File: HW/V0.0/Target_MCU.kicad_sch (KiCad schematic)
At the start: 18 parts, among them SW1 SW-2P, U3 PIC16F877A-I/PT

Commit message: PIC16-DevKit-SCH-877 schematic update 4
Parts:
- added MD1: ARDUINO-UNO-R3, symbol SAMPI:ARDUINO-UNO-R3
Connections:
- net GND: now also MD1.29 (GND), MD1.6 (GND), MD1.7 (GND)
- new net +3.3V: MD1.4 (+3V3)
- new net +5V: MD1.5 (+5V)
- new net VDC: MD1.8 (VIN)

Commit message: PIC16-DevKit-SCH-877 schematic update 5
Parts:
- removed C18: 100nF, symbol Triet_KiCAD_Sym:CAP_CER
- removed R25: 330R, symbol Triet_KiCAD_Sym:RES
- removed Y2: ~, symbol Triet_KiCAD_Sym:Crystal-3P
- added J3: EXP PORT, SAMPI:HDM1x10x2.54_TH_RA, symbol SAMPI:SIL10
- added R11, R12, R14, R15, R16, R19, R20: 330R, SAMPI:RES0603, symbol Triet_KiCAD_Sym:RES
- added U10: 20MHz, SAMPI:CDFN3225-4LD-PL-1, symbol SAMPI:XTAL-4P
- C15: renamed from C16; footprint (none) -> SAMPI:CAP0603
- C16: renamed from C15; footprint (none) -> SAMPI:CAP0603
- C17: footprint (none) -> SAMPI:CAP0603
- C18: renamed from C8; footprint (none) -> SAMPI:CAP0603
- C19: renamed from C9; footprint (none) -> SAMPI:CAP0603
- C20: renamed from C10; footprint (none) -> SAMPI:CAP0603
- C21: renamed from C11; footprint (none) -> SAMPI:CAP0603
- D5: renamed from D4; value PWR -> ULED; footprint (none) -> SAMPI:LED0603
- MD1: footprint (none) -> SAMPI:ARDUINO-UNO-R3
- R13: value 1k -> 330R; footprint (none) -> SAMPI:RES0603
- R17: value 10k -> 330R; footprint (none) -> SAMPI:RES0603
- R18: renamed from R16; value 10k -> 10K; footprint (none) -> SAMPI:RES0603
- R21: renamed from R34; value 4.7k -> 5.1K, 1%; footprint (none) -> SAMPI:RES0603
- R22: renamed from R35; value 4.7k -> 5.1K, 1%; footprint (none) -> SAMPI:RES0603
- SW1: value SW-2P -> UBT; MPN SW603625R2 -> (none)
- U4: renamed from U3; value PIC16F877A-I/PT -> PIC16F877A; footprint (none) -> SAMPI:TQFP44-10x10-P0.8; MFT (none) -> Microchip; MNP (none) -> PIC16F877A-I/PT
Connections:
- net AN4/SCL is gone; now on net GND: U4.6 (VSS)
- net AN5/SDA is gone; now on net +VDDTG: U4.7 (VDD)
- net GPIO2 is gone; now on net INT1: U4.9 (RB1)
- net GPIO3 is gone; now on net INT0: U4.8 (INT/RB0)
- net GPIO5 is gone; now on net SCL: U4.37 (SCK/SCL/RC3)
- net MOSI is gone; now on net AN4: U4.24 (~{SS}/C2OUT/AN4/RA5)
- net RESET is gone; now on net INT2: U4.10 (RB2)
- net RTC_CLKO is gone; now on net SCLK: U4.15 (RB5)
- net RTC_EVI is gone; now on net AN1: U4.20 (AN1/RA1)
- net TG_RXD is gone; now on net ~{UBT}: U4.26 (RE1/~{WR}/AN6)
- net TG_TXD is gone; now on net AN5: U4.25 (RE0/~{RD}/AN5)
- net UART_SEL is gone; now on net AN0: U4.19 (AN0/RA0)
- net ~{FLASH_CS} is gone; now on net AN3: U4.22 (VREF+/AN3/RA3)
- net ~{FLASH_WP} is gone; now on net AN2: U4.21 (CVREF/VREF-/AN2/RA2)
- net ~{RTC_INT} is gone; now on net PWM2: U4.35 (T1OSI/CCP2/RC1)
- net ~{TEMP_OS} is gone; now on net +VDDTG: U4.28 (VDD)
- net ~{TG_PGM}/~{SRAM_CS_3V3} is gone; now on net PWM1: U4.36 (CCP1/RC2)
- net +VDDTG: now also MD1.2 (IOREF), MD1.30 (AREF), J3.2; no longer R17.1, U4.11 (VDD), U4.32 (VDD)
- net AN0: now also MD1.9 (AN0); no longer U4.2 (AN0/RA0)
- net AN1: now also MD1.10 (AN1); no longer U4.3 (AN1/RA1)
- net AN2: now also MD1.11 (AN2); no longer U4.4 (CVref/Vref-/AN2/RA2)
- net AN3: now also MD1.12 (AN3); no longer U4.5 (Vref+/AN3/RA3)
- net GND: now also D5.K, U4.29 (VSS), J3.1, U10.2 (GND1), U10.4 (X2); no longer U4.12 (VSS), U4.31 (VSS)
- net INT0: now also MD1.21 (D6); no longer U4.34 (RB1)
- net INT1: now also MD1.22 (D7); no longer U4.33 (INT/RB0)
- net SCL: now also MD1.32 (D15/SCL); no longer U4.18 (SCK/SCL/RC3)
- net SCLK: now also MD1.28 (D13/SCLK); no longer U4.39 (PGC/RB6)
- net SDA: now also MD1.31 (D14/SDA), U4.42 (SDI/SDA/RC4); no longer U4.23 (SDI/SDA/RC4)
- net ~{CS}: now also MD1.25 (D10/~{SS}), U4.11 (PGM/RB3); no longer U4.27 (RD4/PSP4)
- net AN4: now reaches MD1.13 (AN4/SDA)
- net AN5: now reaches MD1.14 (AN5/SCL)
- net RXD: now reaches MD1.15 (D0/RXD)
- net RXD: now also U4.1 (DT/RX/RC7)
- net TXD: now reaches MD1.16 (D1/TXD)
- net TXD: now also U4.44 (CK/TX/RC6)
- net T0CKI: now reaches MD1.17 (D2)
- net T0CKI: now also U4.23 (C1OUT/T0CKI/RA4)
- net T1CKI: now reaches MD1.18 (D3)
- net T1CKI: now also U4.32 (T1OSO/T1CKI/RC0)
- net ULED: now reaches MD1.19 (D4)
- net ULED: now also U4.27 (RE2/~{CS}/AN7), R19.1
- net INT2: now reaches MD1.20 (D5)
- net PWM1: now reaches MD1.23 (D8)
- net PWM2: now reaches MD1.24 (D9)
- net SDO: now reaches MD1.26 (D11/MOSI)
- net SDO: now also U4.43 (SDO/RC5)
- net SDI: now reaches MD1.27 (D12/MISO)
- net SDI: now also U4.14 (RB4)
- net ~{MCLR}: now reaches MD1.3 (RESET)
- net ~{MCLR}: now also U4.18 (~{MCLR}/VPP)
- net at C15.2: now also U4.30 (OSC1/CLKI), U10.3 (GND2); no longer U4.13 (OSC1/CLKI)
- net ~{UBT}: now reaches C17.2, R18.2, SW1.B
- net ~{UBT}: no longer R13.2
- net at R17.2: now also J3.9; no longer U4.1 (~{MCLR}/Vpp)
- net at C16.2: now also U4.31 (OSC2/CLKO), U10.1 (X1); no longer U4.14 (OSC2/CLKO)
- net GPIO0 renamed PGC
- net GPIO1 renamed PGD
- net GPIO4 renamed RD0
- net RD0: now also R11.1
- net MISO renamed RD2
- net RD2: now also R13.1
- removed net USER_LED: D5.1 (A), U4.29 (RD6/PSP6)
- removed net ~{USER_BT}: R13.1, U4.30 (RD7/PSP7)
- new net: J3.10, R20.2
- new net: J3.3, R11.2
- new net: J3.4, R12.2
- new net: J3.5, R13.2
- new net: J3.6, R14.2
- new net: J3.7, R15.2
- new net: J3.8, R16.2
- new net: D5.A, R19.2
- new net RD1: R12.1, U4.39 (RD1/PSP1)
- new net RD3: R14.1, U4.41 (RD3/PSP3)
- new net RD4: R15.1, U4.2 (RD4/PSP4)
- new net RD5: R16.1, U4.3 (RD5/PSP5)
- new net RD6: R17.1, U4.4 (RD6/PSP6)
- new net RD7: R20.1, U4.5 (RD7/PSP7)
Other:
- moved on the sheet: C15, C16, C17, D5, R18, SW1

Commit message: PIC16-DevKit-SCH-877 schematic update 6
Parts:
- removed SW1: UBT, Triet_KiCAD_Fprint:SW_2P_3.5x6, symbol Triet_KiCAD_Sym:Switch_2P
- added BT2: UBT, Liem:SW6x6-G, symbol SAMPI:BT2
- C15, C16: MFT (none) -> Walsin; MNP (none) -> 0603N220J500CT
- C17, C18, C20: MFT (none) -> Samsung; MNP (none) -> CL10B104KB8NNNC
- C19, C21: MFT (none) -> Samsung; MNP (none) -> CL10A106MQ8NNNC
- D5: MFT (none) -> Harvatek; MNP (none) -> B1911NG--20D000214U1930
- J3: footprint SAMPI:HDM1x10x2.54_TH_RA -> SAMPI:HDM1x10x2.54_TH; MFT (none) -> Adam Tech; MNP (none) -> RS1-10-G
- MD1: MFT (none) -> JLCPCB; MNP (none) -> PCB.SAMM-877A
- R11, R12, R13, R14, R15, R16, R17, R19, R20: MFT (none) -> Yageo; MNP (none) -> RC0603JR-07330RL
- R18: MFT (none) -> Yageo; MNP (none) -> RC0603JR-0710KL
- R21, R22: MFT (none) -> Yageo; MNP (none) -> RC0603FR-075K1L
- U10: MFT (none) -> Diodes; MNP (none) -> FL2000038
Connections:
- net GND: now also BT2.3, BT2.4
- net ~{UBT}: now also BT2.1, BT2.2
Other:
- moved on the sheet: C17, R18

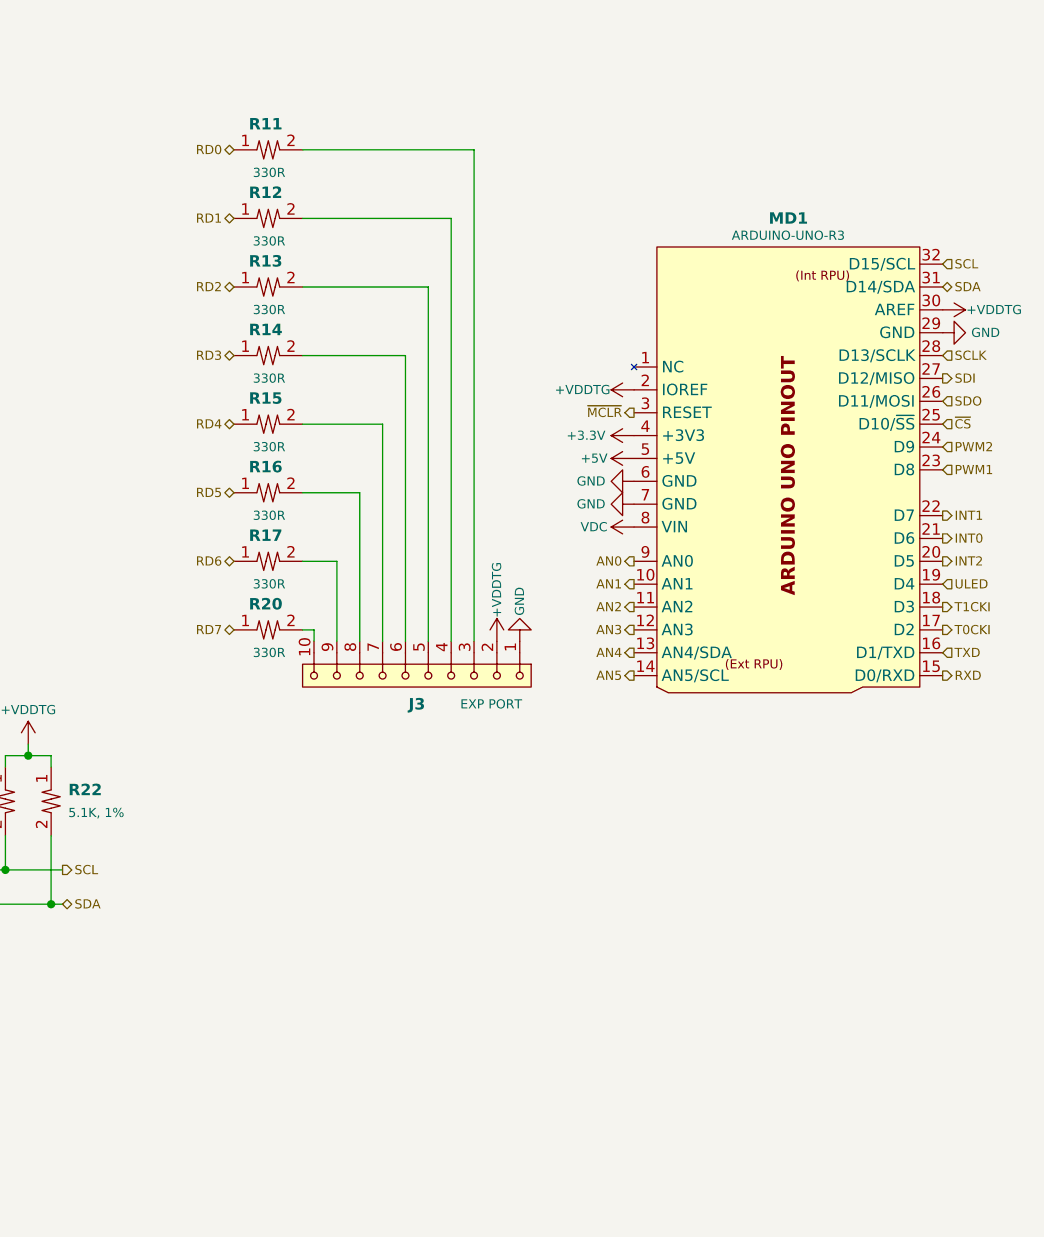
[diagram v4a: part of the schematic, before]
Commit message: PIC16-DevKit-SCH-877 schematic update 7
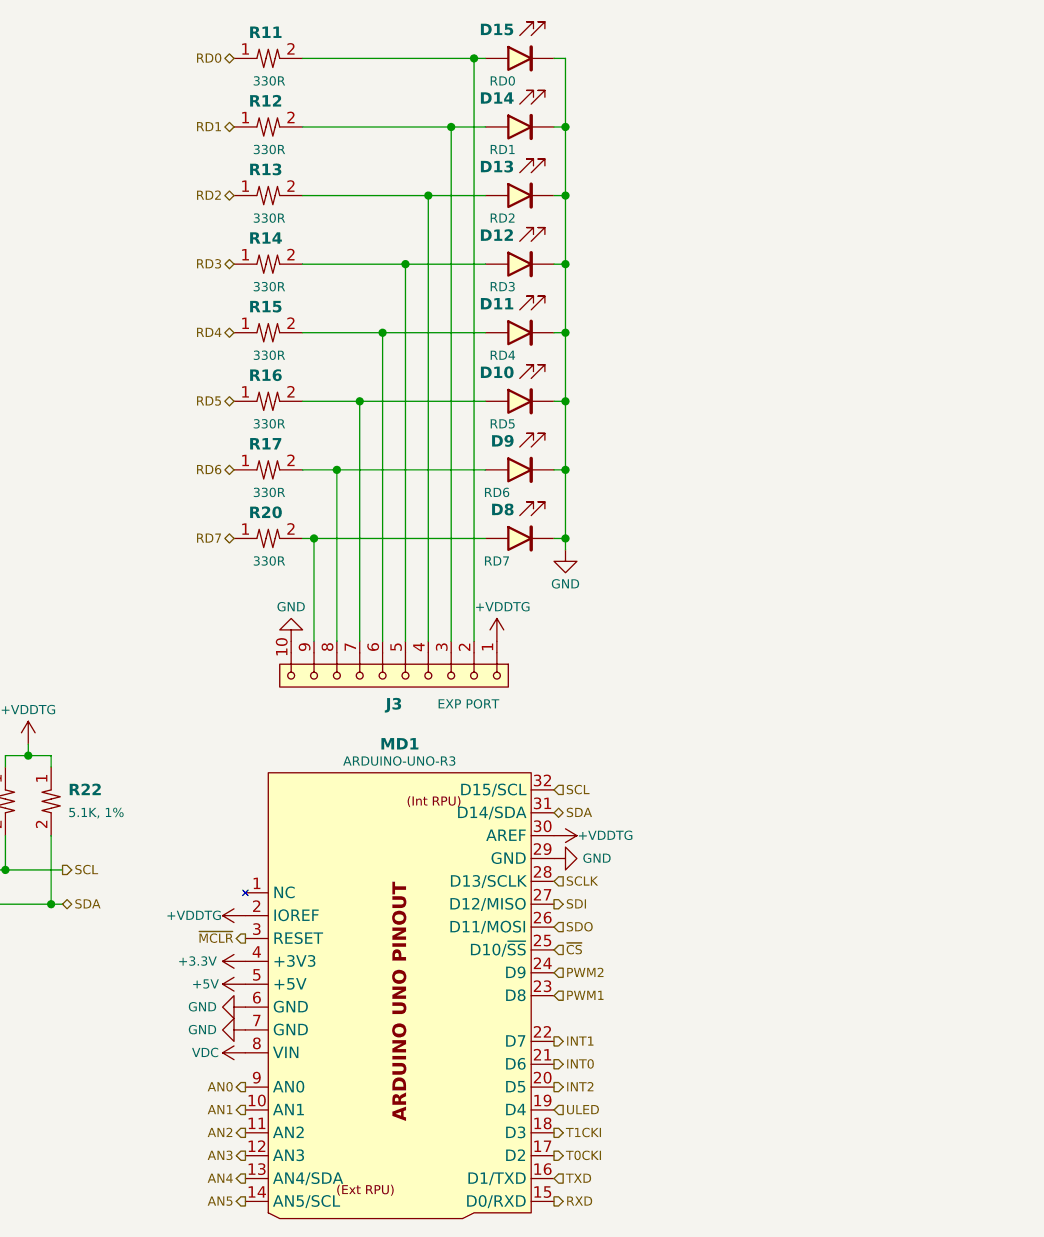
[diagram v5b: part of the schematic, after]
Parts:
- added D10: RD5, SAMPI:LED0603, symbol Triet_KiCAD_Sym:LED
- added D11: RD4, SAMPI:LED0603, symbol Triet_KiCAD_Sym:LED
- added D12: RD3, SAMPI:LED0603, symbol Triet_KiCAD_Sym:LED
- added D13: RD2, SAMPI:LED0603, symbol Triet_KiCAD_Sym:LED
- added D14: RD1, SAMPI:LED0603, symbol Triet_KiCAD_Sym:LED
- added D15: RD0, SAMPI:LED0603, symbol Triet_KiCAD_Sym:LED
- added D8: RD7, SAMPI:LED0603, symbol Triet_KiCAD_Sym:LED
- added D9: RD6, SAMPI:LED0603, symbol Triet_KiCAD_Sym:LED
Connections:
- net +VDDTG: now also J3.1; no longer J3.2
- net GND: now also J3.10, D10.K, D11.K, D12.K, D13.K, D14.K, D15.K, D8.K, D9.K; no longer J3.1
- net at R20.2: now also J3.9, D8.A; no longer J3.10
- net at R11.2: now also J3.2, D15.A; no longer J3.3
- net at R12.2: now also J3.3, D14.A; no longer J3.4
- net at J3.5: now also R14.2, D12.A; no longer R13.2
- net at J3.6: now also R15.2, D11.A; no longer R14.2
- net at J3.7: now also R16.2, D10.A; no longer R15.2
- net at J3.8: now also R17.2, D9.A; no longer R16.2
- new net: D13.A, J3.4, R13.2
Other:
- moved on the sheet: MD1, R11, R12, R13, R14, R15, R16, R17, R20

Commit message: PIC16-DevKit-PCB-877 layout update 1
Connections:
- net GND: now also R19.2; no longer D5.K
- net ULED: now also D5.A; no longer R19.1
- new net: D5.K, R19.1
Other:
- moved on the sheet: D5, R19
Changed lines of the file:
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@@
 	(wire
 		(pts
-			(xy 46.99 83.82) (xy 46.99 86.36)
-		)
-		(stroke
-			(width 0)
-			(type default)
-		)
-	)
-	(wire
-		(pts
 			(xy 195.58 49.53) (xy 195.58 57.15)
 		)
@@
 	(hierarchical_label "ULED"
 		(shape input)
-		(at 46.99 76.2 90)
+		(at 46.99 80.645 90)
 		(fields_autoplaced yes)
 		(effects
@@
 	(symbol
 		(lib_id "Triet_KiCAD_Sym:RES")
-		(at 46.99 80.01 0)
+		(at 46.99 92.075 0)
 		(unit 1)
 		(exclude_from_sim no)
@@
 		(dnp no)
 		(property "Reference" "R19"
-			(at 49.53 78.7399 0)
+			(at 49.53 90.8049 0)
 			(effects
 				(font
@@
 		)
 		(property "Value" "330R"
-			(at 49.53 81.28 0)
+			(at 49.53 93.345 0)
 			(effects
 				(font
@@
 		)
 		(property "Footprint" "SAMPI:RES0603"
-			(at 46.99 80.264 90)
+			(at 46.99 92.329 90)
 			(effects
 				(font
@@
 		)
 		(property "Datasheet" ""
-			(at 46.99 80.264 90)
+			(at 46.99 92.329 90)
 			(effects
 				(font
@@
 		)
 		(property "Description" "RES 330R OHM 5% 1/10W 0603"
-			(at 58.42 80.01 0)
+			(at 58.42 92.075 0)
 			(effects
 				(font
@@
 		)
 		(property "MFT" "Yageo"
-			(at 46.99 80.01 0)
+			(at 46.99 92.075 0)
 			(effects
 				(font
@@
 		)
 		(property "MNP" "RC0603JR-07330RL"
-			(at 46.99 80.01 0)
+			(at 46.99 92.075 0)
 			(effects
 				(font
@@
 	(symbol
 		(lib_id "power:GND")
-		(at 46.99 93.98 0)
+		(at 46.99 95.885 0)
 		(unit 1)
 		(exclude_from_sim no)
@@
 		(dnp no)
 		(property "Reference" "#PWR052"
-			(at 46.99 100.33 0)
+			(at 46.99 102.235 0)
 			(effects
 				(font
@@
 		)
 		(property "Value" "GND"
-			(at 46.99 97.79 0)
+			(at 46.99 99.695 0)
 			(effects
 				(font
@@
 		)
 		(property "Footprint" ""
-			(at 46.99 93.98 0)
+			(at 46.99 95.885 0)
 			(effects
 				(font
@@
 		)
 		(property "Datasheet" ""
-			(at 46.99 93.98 0)
+			(at 46.99 95.885 0)
 			(effects
 				(font
@@
 		)
 		(property "Description" "Power symbol creates a global label with name \"GND\" , ground"
-			(at 46.99 93.98 0)
+			(at 46.99 95.885 0)
 			(effects
 				(font
@@
 		)
 		(instances
-			(project ""
+			(project "PIC16DevKit"
 				(path "/17281b91-3f9a-4e36-96b2-66002b412b3a/dceb7a93-1172-4461-96bc-c129bdd90128"
 					(reference "U10")
@@
 		(lib_name "LED_2")
 		(lib_id "Triet_KiCAD_Sym:LED")
-		(at 46.99 90.17 270)
+		(at 46.99 84.455 270)
 		(unit 1)
 		(exclude_from_sim no)
@@
 		(fields_autoplaced yes)
 		(property "Reference" "D5"
-			(at 52.07 89.5984 90)
+			(at 52.07 83.8834 90)
 			(effects
 				(font
@@
 		)
 		(property "Value" "ULED"
-			(at 52.07 92.1385 90)
+			(at 52.07 86.4235 90)
 			(effects
 				(font
@@
 		)
 		(property "Footprint" "SAMPI:LED0603"
-			(at 43.815 90.17 0)
+			(at 43.815 84.455 0)
 			(effects
 				(font
@@
 		)
 		(property "Datasheet" ""
-			(at 46.99 90.17 0)
+			(at 46.99 84.455 0)
 			(effects
 				(font
@@
 		)
 		(property "Description" "LED GREEN DIFFUSED 0603 SMD"
-			(at 46.99 90.17 0)
+			(at 46.99 84.455 0)
 			(effects
 				(font
@@
 		)
 		(property "MFT" "Harvatek"
-			(at 46.99 90.17 0)
+			(at 46.99 84.455 0)
 			(effects
 				(font
@@
 		)
 		(property "MNP" "B1911NG--20D000214U1930"
-			(at 46.99 90.17 0)
+			(at 46.99 84.455 0)
 			(effects
 				(font
